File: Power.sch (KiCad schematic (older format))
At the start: 17 parts

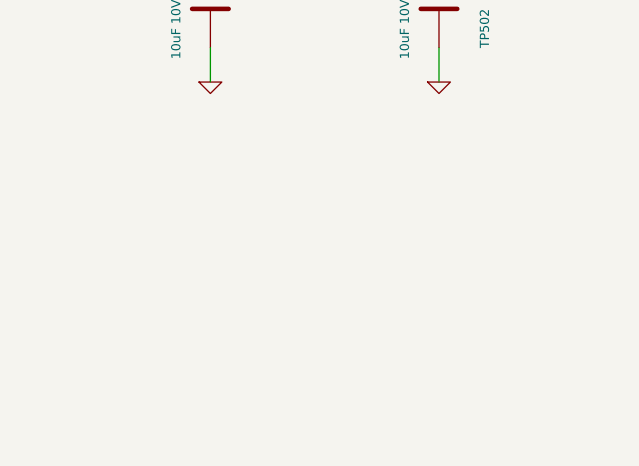
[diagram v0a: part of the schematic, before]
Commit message: Add 4 additional 3.3V decoupling capacitors for the 3.3V power plane
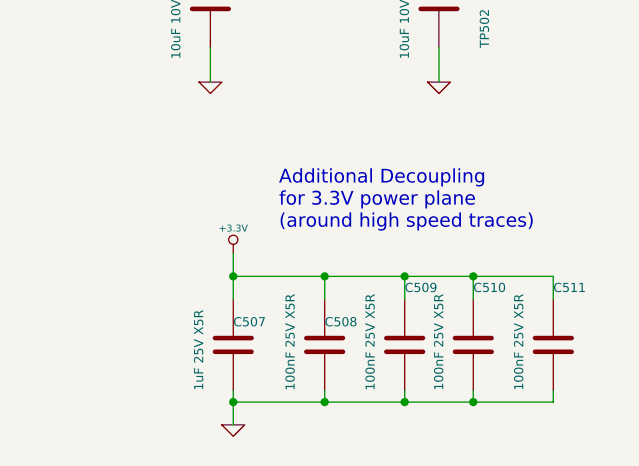
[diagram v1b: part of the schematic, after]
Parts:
- added C507: 1uF 25V X5R, SMD_Packages:SMD-0402_c, symbol C
- added C508, C509, C510, C511: 100nF 25V X5R, SMD_Packages:SMD-0402_c, symbol C
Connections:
- net +3.3V: now also C507.1, C508.1, C509.1, C510.1, C511.1
- net GND: now also C507.2, C508.2, C509.2, C510.2, C511.2
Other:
- note added: "Additional Decoupling\nfor 3.3V power plane\n(around high speed traces)"
